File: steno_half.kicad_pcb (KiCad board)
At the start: 2 copper layers, 144 x 90.8 mm, 38 parts, among them J1 IDC-Header_2x05_P2.54mm_Verti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, J2 IDC-Header_2x05_P2.54mm_Verti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

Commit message: Adicionados botões e leds e roteado. Em princípio, pronto para fabricar. Interessante remover os erros de DRC restantes, causados pelo footprint do STM 32 Blue Pill.
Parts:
- added BTN1: SW_PUSH_6mm, Button_Switch_THT:SW_PUSH_6mm, B.Cu at (148.7, 117.0)
- added BTN2: SW_PUSH_6mm, Button_Switch_THT:SW_PUSH_6mm, B.Cu at (149.0, 149.5)
- added BTN3: SW_PUSH_6mm, Button_Switch_THT:SW_PUSH_6mm, B.Cu at (148.8, 159.5)
- added D15: D_SOD-123, Diode_SMD:D_SOD-123, F.Cu at (146.5, 171.0)
- added D16: D_SOD-123, Diode_SMD:D_SOD-123, F.Cu at (145.5, 144.0)
- added D17: D_SOD-123, Diode_SMD:D_SOD-123, F.Cu at (145.5, 124.5)
- added GRN: LED_D3.0mm, LED_THT:LED_D3.0mm, B.Cu at (143.8, 136.0)
- added RED: LED_D3.0mm, LED_THT:LED_D3.0mm, B.Cu at (150.3, 136.0)
- added R_GRN: R_0805_2012Metric, Resistor_SMD:R_0805_2012Metric, F.Cu at (146.0, 141.0)
- added R_RED: R_0805_2012Metric, Resistor_SMD:R_0805_2012Metric, F.Cu at (146.0, 129.5)
- renumbered REF** to H1, REF** to H2, REF** to H3, REF** to H4, REF** to H5, REF** to H6, REF** to H7
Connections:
- STM32 Blue Pill pad 21: (no net) -> GND
- STM32 Blue Pill pad 3: (no net) -> R2
- STM32 Blue Pill pad 4: (no net) -> LED_RED_GPIO
- STM32 Blue Pill pad 5: (no net) -> LED_GRN_GPIO
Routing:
- net R1: track 0.00 -> 255.3 mm, vias 0 -> 2
- net R0: track 0.00 -> 216.0 mm, vias 0 -> 2
- net C5: track 0.00 -> 183.4 mm, vias 0 -> 1
- net C4: track 0.00 -> 174.7 mm
- net C3: track 0.00 -> 155.3 mm
- net C2: track 0.00 -> 141.0 mm, vias 0 -> 1
- net C0: track 0.00 -> 122.3 mm
- net C1: track 0.00 -> 121.4 mm, vias 0 -> 1
- net C6: track 0.00 -> 94.5 mm
- net R2: track 0.00 -> 70.4 mm, vias 0 -> 3
- net X8: track 0.00 -> 51.0 mm
- net X7: track 0.00 -> 40.2 mm
- net X2: track 0.00 -> 39.2 mm, vias 0 -> 1
- net X6: track 0.00 -> 39.0 mm
- net X9: track 0.00 -> 38.4 mm, vias 0 -> 1
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
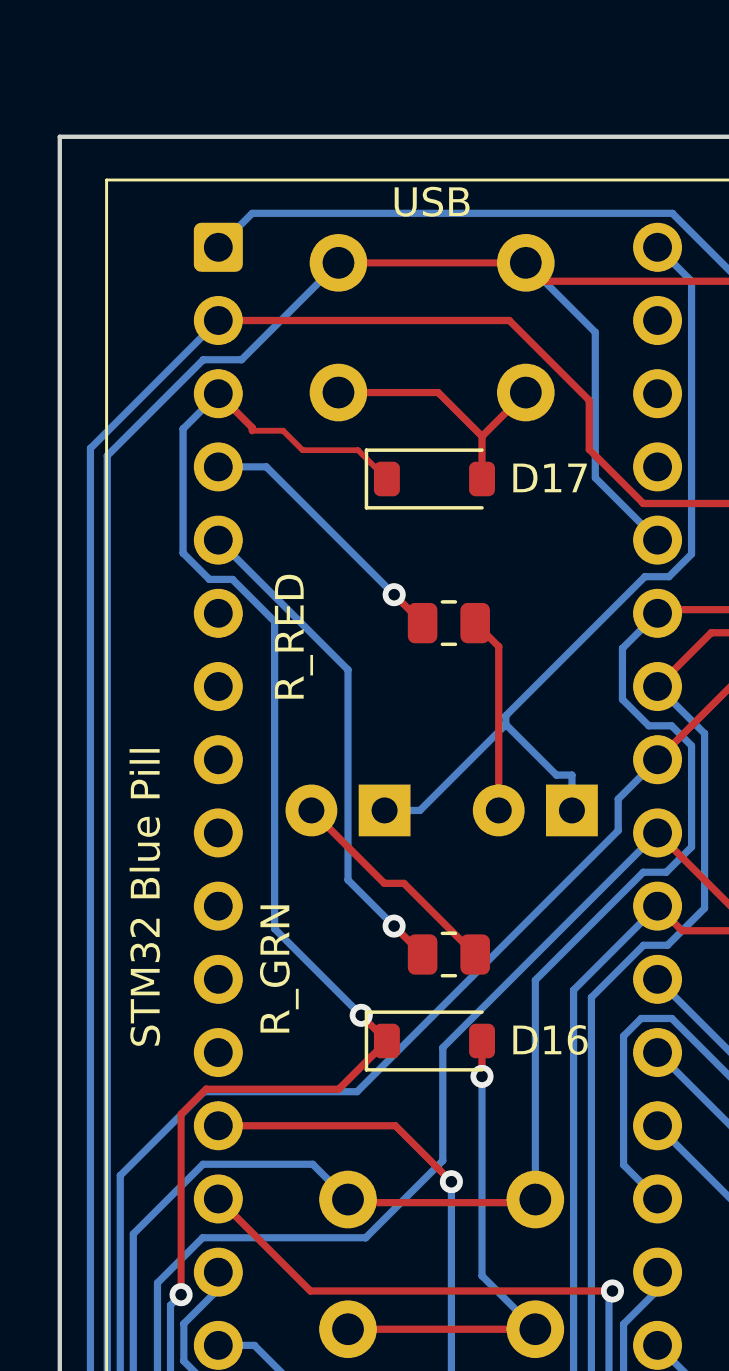
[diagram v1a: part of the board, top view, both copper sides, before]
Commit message: Alterado o footprint do Blue Pill (sem erros de DRC). Readicionando biblioteca de switches. Adicionando arquivos de exportação (grb, drl, etc.).
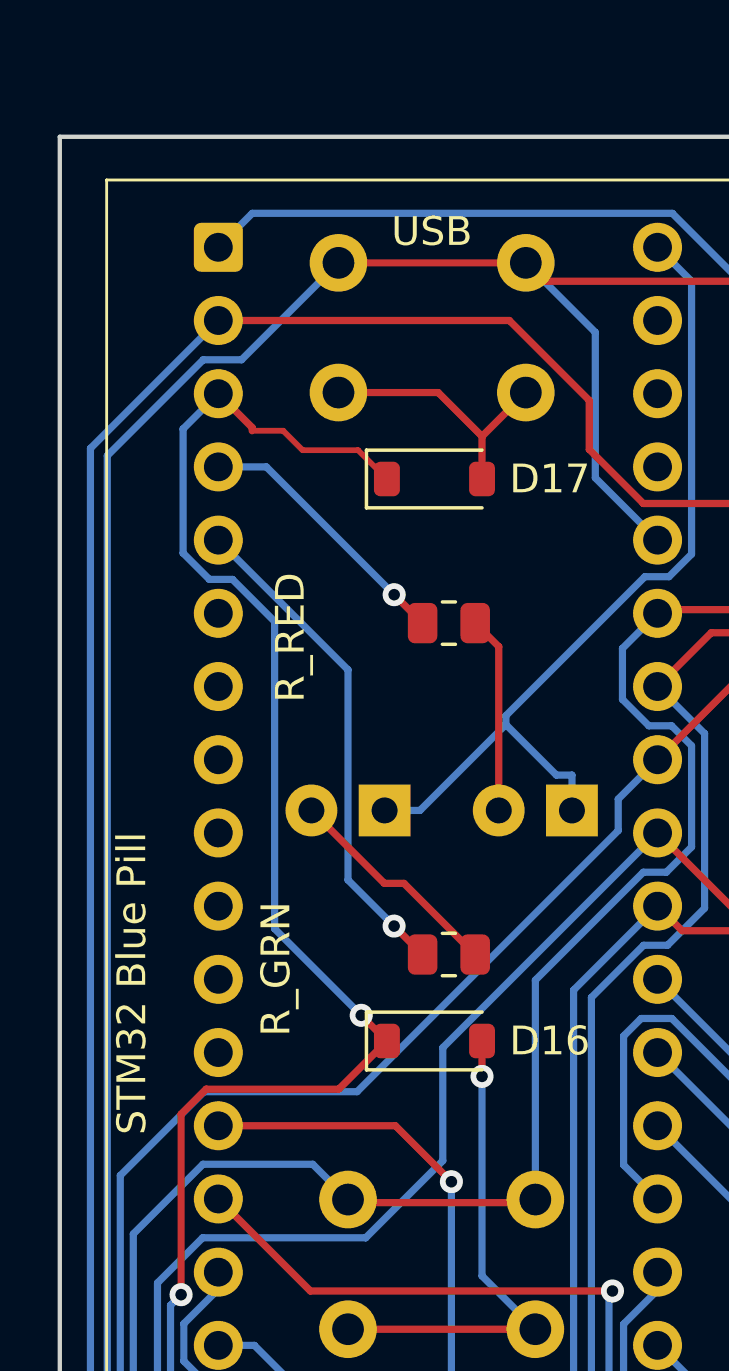
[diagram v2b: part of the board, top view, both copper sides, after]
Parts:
- STM32 Blue Pill: value STM32BluePill_2x20_P2.54mm -> STM32BluePill_2x20_P2.54mm_socketed; footprint keyboard-parts-global:STM32BluePill_2x20_P2.54mm -> keyboard-parts-global:STM32BluePill_2x20_P2.54mm_socketed
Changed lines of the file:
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@@
 		(capping no)
 		(filling no)
-		(zone_defaults)
 		(pcbplotparams
 			(layerselection 0x00000000_00000000_55555555_5755f5ff)
@@
 			(outputformat 1)
 			(mirror no)
-			(drillshape 1)
+			(drillshape 0)
 			(scaleselection 1)
-			(outputdirectory "")
+			(outputdirectory "outputs-to-fab/")
 		)
 	)
@@
 		(embedded_fonts no)
 	)
-	(footprint "keyboard-parts-global:STM32BluePill_2x20_P2.54mm"
+	(footprint "keyboard-parts-global:STM32BluePill_2x20_P2.54mm_socketed"
 		(layer "F.Cu")
 		(at 138 116.5)
 		(property "Reference" "STM32 Blue Pill"
-			(at -2.5 22.5 90)
+			(at -3 25.5 90)
 			(unlocked yes)
 			(layer "F.SilkS")
@@
 			)
 		)
-		(property "Value" "STM32BluePill_2x20_P2.54mm"
+		(property "Value" "STM32BluePill_2x20_P2.54mm_socketed"
 			(at 0 -5.5 0)
 			(unlocked yes)
@@
 		)
 		(fp_rect
-			(start -4.75 -3.25)
-			(end 20 51.5)
+			(start -1.5 -1.54)
+			(end 1.5 49.8)
+			(stroke
+				(width 0.05)
+				(type default)
+			)
+			(fill no)
+			(layer "F.CrtYd")
+		)
+		(fp_rect
+			(start 13.74 -1.54)
+			(end 16.74 49.8)
 			(stroke
 				(width 0.05)
@@
 		)
 		(fp_text user "USB"
-			(at 6 -1 0)
+			(at 6 0 0)
 			(unlocked yes)
 			(layer "F.SilkS")
@@
 	)
 	(segment
-		(start 147.73 136)
-		(end 147.73 130.3175)
-		(width 0.25)
-		(layer "F.Cu")
-		(net "LED_RED_A")
-	)
-	(segment
-		(start 147.73 130.3175)
-		(end 146.9125 129.5)
-		(width 0.25)
-		(layer "F.Cu")
-		(net "LED_RED_A")
-	)
-	(segment
 		(start 142.5 154)
 		(end 149 154)
@@
 		(net "ts_top")
 	)
+	(segment
+		(start 147.73 136)
+		(end 147.73 130.3175)
+		(width 0.25)
+		(layer "F.Cu")
+		(net "LED_RED_A")
+	)
+	(segment
+		(start 147.73 130.3175)
+		(end 146.9125 129.5)
+		(width 0.25)
+		(layer "F.Cu")
+		(net "LED_RED_A")
+	)
 	(embedded_fonts no)
